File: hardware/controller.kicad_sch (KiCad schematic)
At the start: 1 part, among them U1 ESP32-C6-WROOM-1

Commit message: :construction: daily update
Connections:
- net LED_DATA renamed TOMO0
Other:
- moved on the sheet: U1

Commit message: :construction: controller position
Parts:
- added FPC1: ~, KeysDock:AFC01-S16FCA-00, symbol components:FPC-SMD_AFC01-S16FCA
- added J1: Connector, USB-TYPE-C-16P, KeysDock:TYPE-C-SMD_HX-TYPE-C-16PIN, symbol components:Connector, USB-TYPE-C-16P
- added PC1: ~, KeysDock:ZX-ZH1.5-3PWT, symbol components:ZX-ZH1.5-3PWT
- added PC2: ~, KeysDock:ZX-ZH1.5-2PWT, symbol components:ZX-ZH1.5-2PWT
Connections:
- new net: J1.A12B1 (GND), J1.B12A1 (GND)
- new net: J1.A9B4 (VBUS), J1.B9A4 (VBUS)

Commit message: :construction: some connectors
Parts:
- added PC3: ~, KeysDock:ZX-ZH1.5-3PWT, symbol components:ZX-ZH1.5-3PWT
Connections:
- net P,+3.3: now also PC1.3 (Y3), PC2.2 (Y2)
- net P,E: now also J1.A12B1 (GND), J1.B12A1 (GND), PC1.2 (Y2), PC2.1 (Y1), PC3.3 (Y3)
- net U0RX: now also PC3.2 (Y2)
- net U0TX: now also PC3.1 (Y1)
- net P,+5: now reaches PC1.1 (Y1)
- no-connect marks 0 -> 9
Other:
- moved on the sheet: FPC1, J1, PC1

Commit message: :sparkles: add some components
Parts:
- added C1, C3: 10uF, KeysDock:C_0402, symbol components:0402,10uF
- added C2, C4, C5, C6, C7: 100nF, KeysDock:C_0402, symbol components:0402,100nF
- added U2: ~, KeysDock:TLV1117LV33DCYR, symbol components:TLV1117LV33DCYR
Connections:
- net P,+3.3: now also C1.1, C2.1, C4.1, C5.1, C6.1, C7.1, U2.2 (OUT), U2.4 (OUT); no longer PC2.2 (Y2)
- net P,+5: now also PC2.2 (Y2), C3.1, U2.3 (IN)
- net P,E: now also C1.2, C2.2, C3.2, C4.2, C5.2, C6.2, C7.2, U2.1 (ADJ/GND)
- net U0RX: now also PC3.1 (Y1); no longer PC3.2 (Y2)
- net U0TX: now also PC3.2 (Y2); no longer PC3.1 (Y1)

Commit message: :construction: sync components
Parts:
- removed C1, C3: 10uF, KeysDock:C_0402, symbol components:0402,10uF
- removed C2: 100nF, KeysDock:C_0402, symbol components:0402,100nF
- removed U2: ~, KeysDock:TLV1117LV33DCYR, symbol components:TLV1117LV33DCYR
- added C10: 22uF, KeysDock:C_0603, symbol components:0603,22uF
- added C8: 4.7uF, KeysDock:C_0402, symbol components:0402,4.7uF
- added C9: 10uF, KeysDock:C_0402, symbol components:0402,10uF
- added L1: 22uH,5mA, KeysDock:IND-SMD_L2.5-W2.0_MHCHL2520, symbol components:FTC252012S2R2MBCA
- added R3: 267kΩ, KeysDock:R_0402, symbol components:0402,267kΩ
- added U3: TPS62840YBGR, KeysDock:BGA6N40P3X2_146X96X50N, symbol components:TPS62840YBGR
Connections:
- new net: R3.2, U3.C2 (VSET)
- new net: L1.1, U3.B2 (SW)
- new net +3.3V: C10.1, C9.1, L1.2, U3.A2 (VOS)
- new net +5V: C8.1, U3.B1 (VIN), U3.C1 (EN)
- new net GND: C10.2, C8.2, C9.2, R3.1, U3.A1 (GND)

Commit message: :construction: typeboard routing
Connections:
- net BOOT_1/RANA_SLEEP renamed BOOT_1/RANA
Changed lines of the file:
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@@
 		)
 	)
-	(label "BOOT_1{slash}RANA_SLEEP"
+	(label "BOOT_1{slash}RANA"
 		(at 259.08 91.44 180)
 		(effects

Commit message: :construction: try controller
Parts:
- added D1, D2: SM4007PL, KeysDock:D_SOD-123FL, symbol components:SM4007PL
- added PC4: ~, KeysDock:ZX-ZH1.5-3PWT, symbol components:ZX-ZH1.5-3PWT
- added R1: 100Ω, KeysDock:R_0402, symbol components:0402,100Ω
- added S2: Tactile Button, 160gf, KeysDock:SW_TS-1088-AR02016, symbol components:Tactile Button, 160gf, 12V, 50mA, 4.0mm
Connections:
- net BOOT_0/KEYS_CH_CE: now also D2.2 (A), S2.2 (B)
- net BOOT_1/RANA: now also D1.2 (A)
- net KEYS_CH_A: now also FPC1.1 (Y1)
- net KEYS_CH_B: now also FPC1.2 (Y2)
- net KEYS_CH_C: now also FPC1.3 (Y3)
- net KEYS_CH_D: now also FPC1.4 (Y4)
- net KEYS_DT_1: now also FPC1.12 (Y12)
- net KEYS_DT_2: now also FPC1.13 (Y13)
- net KEYS_DT_3: now also FPC1.14 (Y14)
- net KEYS_DT_4: now also FPC1.15 (Y15)
- net KEYS_DT_5: now also FPC1.16 (Y16)
- net P,E: now also FPC1.11 (Y11), FPC1.6 (Y6), PC3.2 (Y2), PC4.2 (Y2), R1.2; no longer PC3.3 (Y3)
- net SAKI_MOVE: now also FPC1.10 (Y10)
- net TOMO0: now also FPC1.8 (Y8)
- net U0TX: now also PC3.3 (Y3); no longer PC3.2 (Y2)
- net KEYS_CH_CE: now reaches FPC1.5 (Y5)
- net KEYS_CH_CE: now also D2.1 (K)
- net RANA: now reaches FPC1.7 (Y7)
- net RANA: now also D1.1 (K)
- new net: R1.1, S2.1 (A)
- new net BOOT_0: PC4.1 (Y1)
- new net BOOT_1: PC4.3 (Y3)
- no-connect marks 9 -> 12
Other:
- note added: "Boot Mode Button"
- moved on the sheet: PC1, PC3

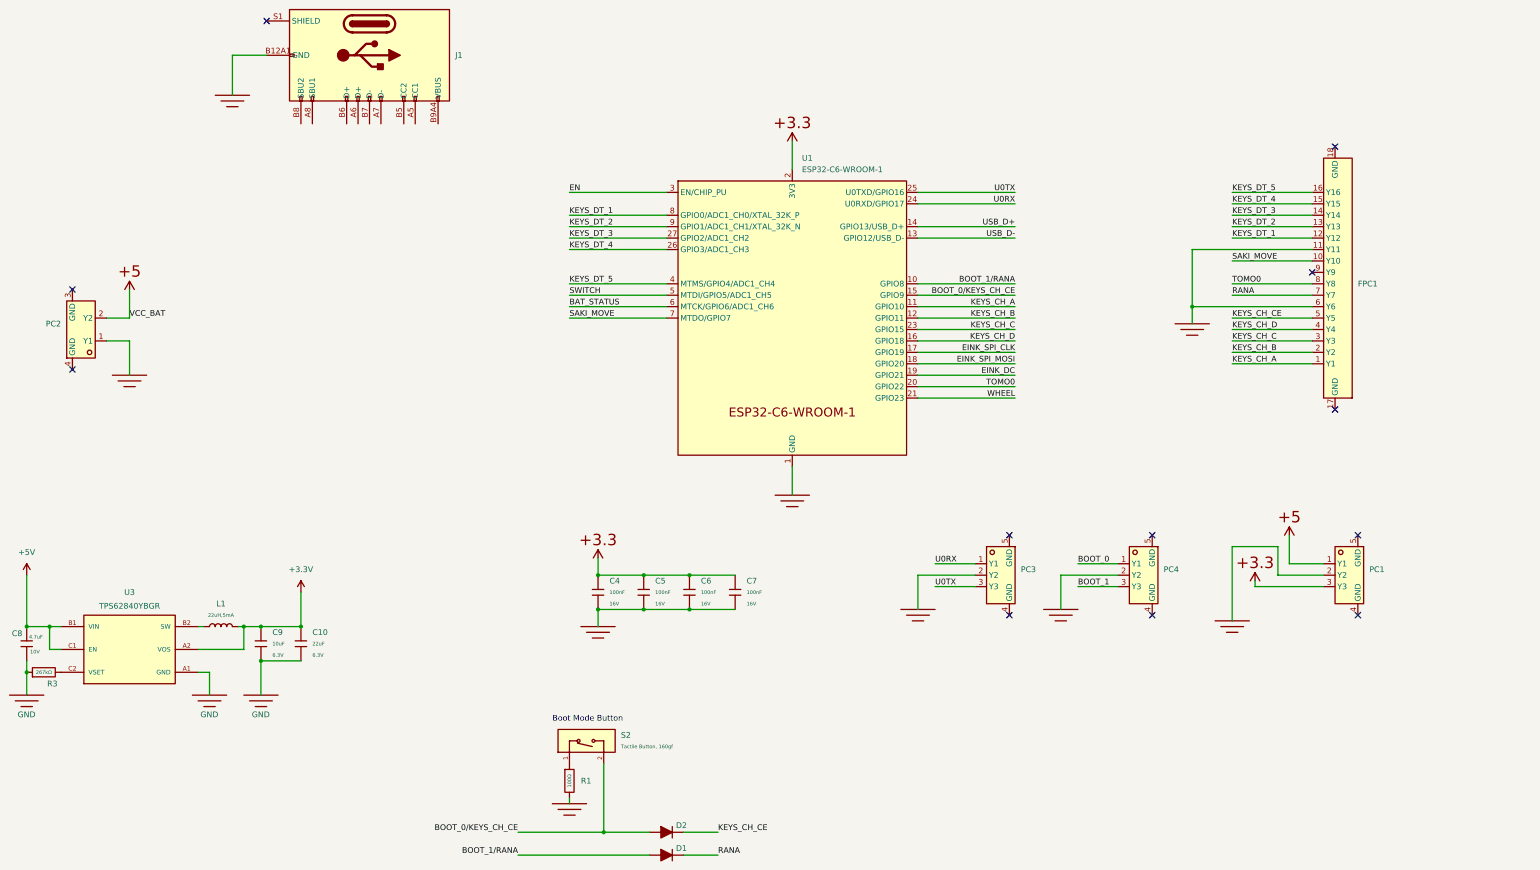
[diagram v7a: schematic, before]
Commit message: :construction: add 4 layer
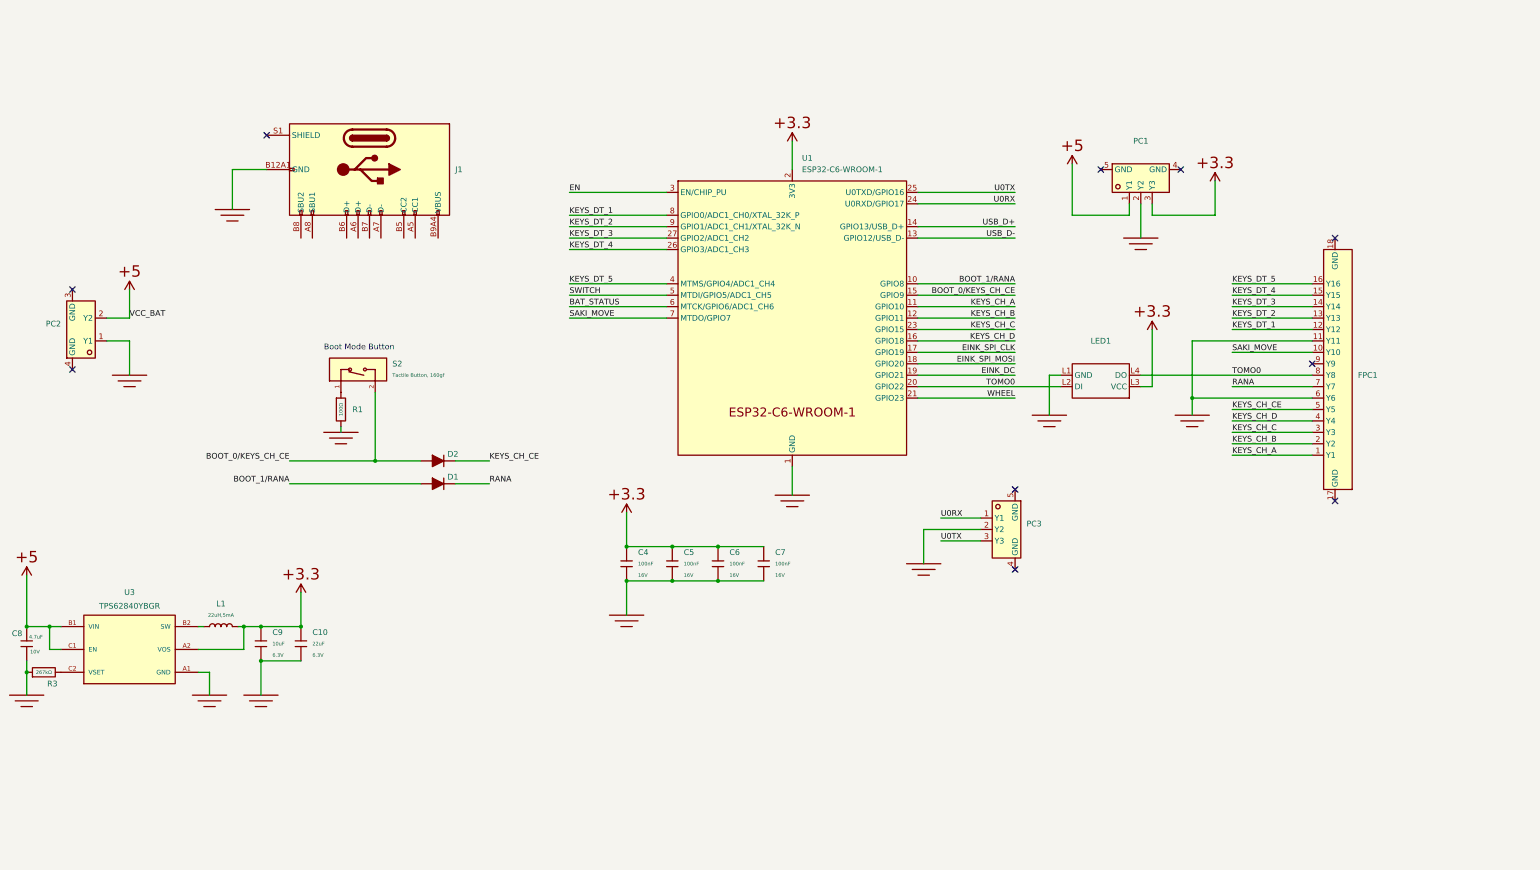
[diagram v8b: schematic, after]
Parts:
- removed PC4: ~, KeysDock:ZX-ZH1.5-3PWT, symbol components:ZX-ZH1.5-3PWT
- added LED1: ~, KeysDock:XL-6028RGBW-WS2812B, symbol components:XL-6028RGBW-WS2812B
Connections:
- net P,+3.3: now also LED1.L3 (VCC)
- net P,E: now also LED1.L1 (GND)
- net TOMO0: now also LED1.L2 (DI), LED1.L4 (DO)
- no-connect marks 12 -> 10
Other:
- moved on the sheet: C4, C5, C6, C7, D1, D2, FPC1, J1, PC1, PC3, R1, S2
